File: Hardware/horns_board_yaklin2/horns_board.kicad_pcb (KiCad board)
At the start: 2 copper layers, 33 x 27 mm, 19 parts, among them J1 Power In, J2 Horn Ctrl, J3 Horn Out 2, J4 Horn Out 1, Q1 NMOS

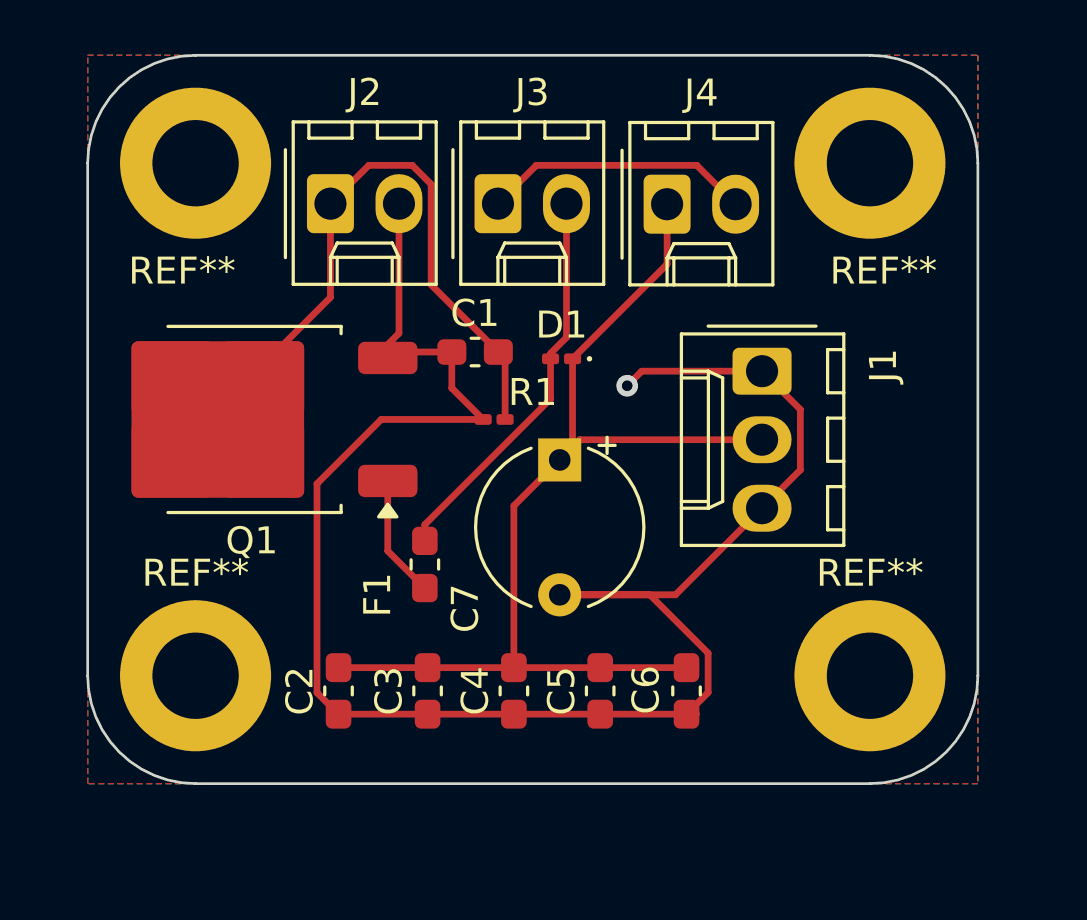
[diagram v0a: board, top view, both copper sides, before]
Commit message: Updated according to comments
Split schematic into multiple modules instead of a single loop.
Replaced Molex kk254 connectors with micro fit and rerouted the traces accordingly.
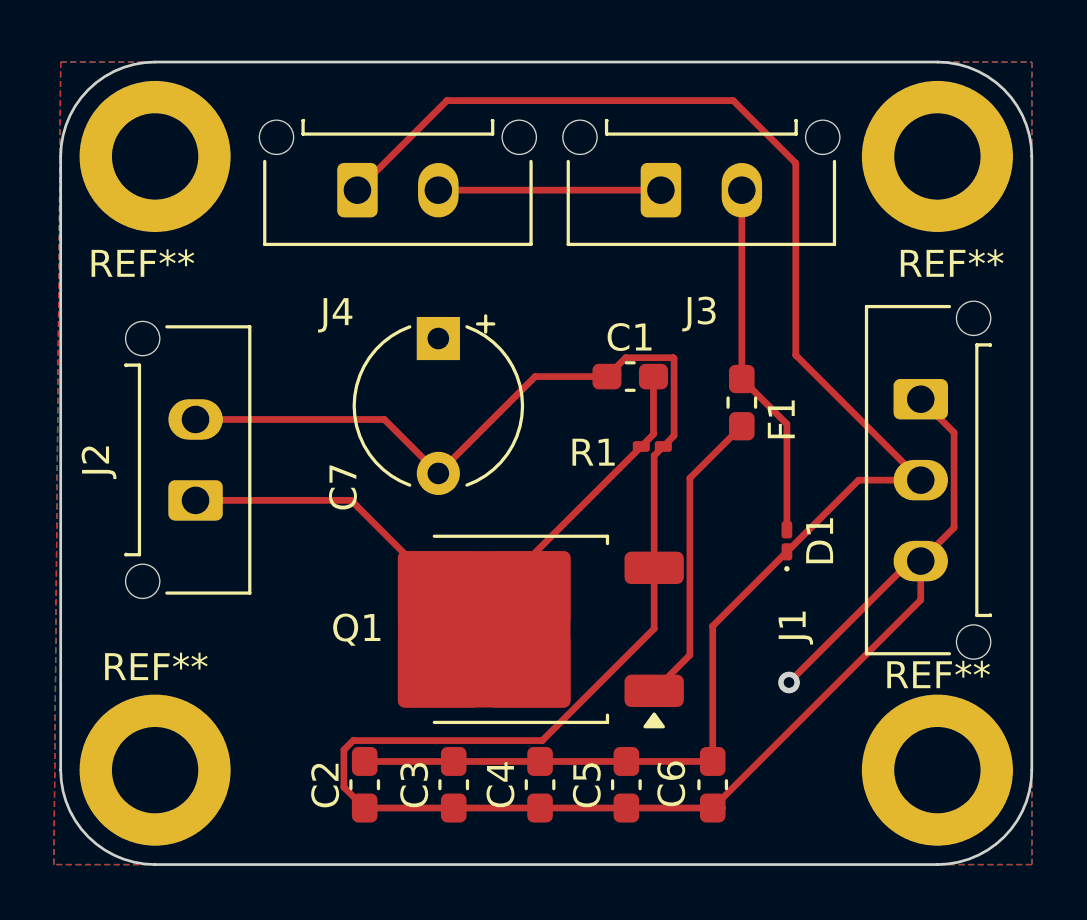
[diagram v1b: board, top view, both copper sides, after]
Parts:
- J1: footprint Connector_Molex:Molex_KK-254_AE-6410-03A_1x03_P2.54mm_Vertical -> Connector_Molex:Molex_Micro-Fit_3.0_43650-0315_1x03_P3.00mm_Vertical
- J2, J3, J4: footprint Connector_Molex:Molex_KK-254_AE-6410-02A_1x02_P2.54mm_Vertical -> Connector_Molex:Molex_Micro-Fit_3.0_43650-0215_1x02_P3.00mm_Vertical
- moved F1 13.2 mm to (118.2, 93.9)
- moved Q1 12.6 mm to (110.0, 102.3)
- moved J2 12.1 mm to (98.0, 97.5), turned to 90 degrees
- moved J4 11.5 mm to (104.0, 86.0)
- moved D1 10.7 mm to (119.9, 99.0), turned to 90 degrees
- moved C7 6.36 mm to (107.0, 91.5)
- moved J3 6.06 mm to (115.2, 86.0)
- moved J1 5.97 mm to (124.9, 93.8)
- moved R1 5.95 mm to (114.9, 95.5), turned to 180 degrees
- moved C1 5.82 mm to (114.1, 92.9)
- moved REF** 4.30 mm to (125.5, 107.5)
- moved REF** 3.81 mm to (96.5, 107.5)
- moved C2 3.61 mm to (104.3, 108.0)
- moved C3 3.61 mm to (107.6, 108.0)
- moved C4 3.61 mm to (110.8, 108.0)
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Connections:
- net Net-(D1-A) renamed Horn In
- net Net-(J2-Pin_1) renamed Horn Ctrl
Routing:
- net +24V: track 40.9 -> 60.4 mm
- net GND: track 71.6 -> 86.4 mm
- net Net-(Q1-D): track 4.54 -> 11.2 mm
- net Horn Ctrl: track 26.2 -> 20.5 mm
- net Net-(J3-Pin_1): track 9.99 -> 8.31 mm
- net Horn In: track 14.7 -> 13.9 mm
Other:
- board size 33 x 27 mm -> 36 x 29.8 mm
